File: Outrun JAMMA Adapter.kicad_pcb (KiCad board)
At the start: 2 copper layers, 111 x 77.8 mm, 24 parts, among them U1 LM386, U2 MCP4902, U4 328P

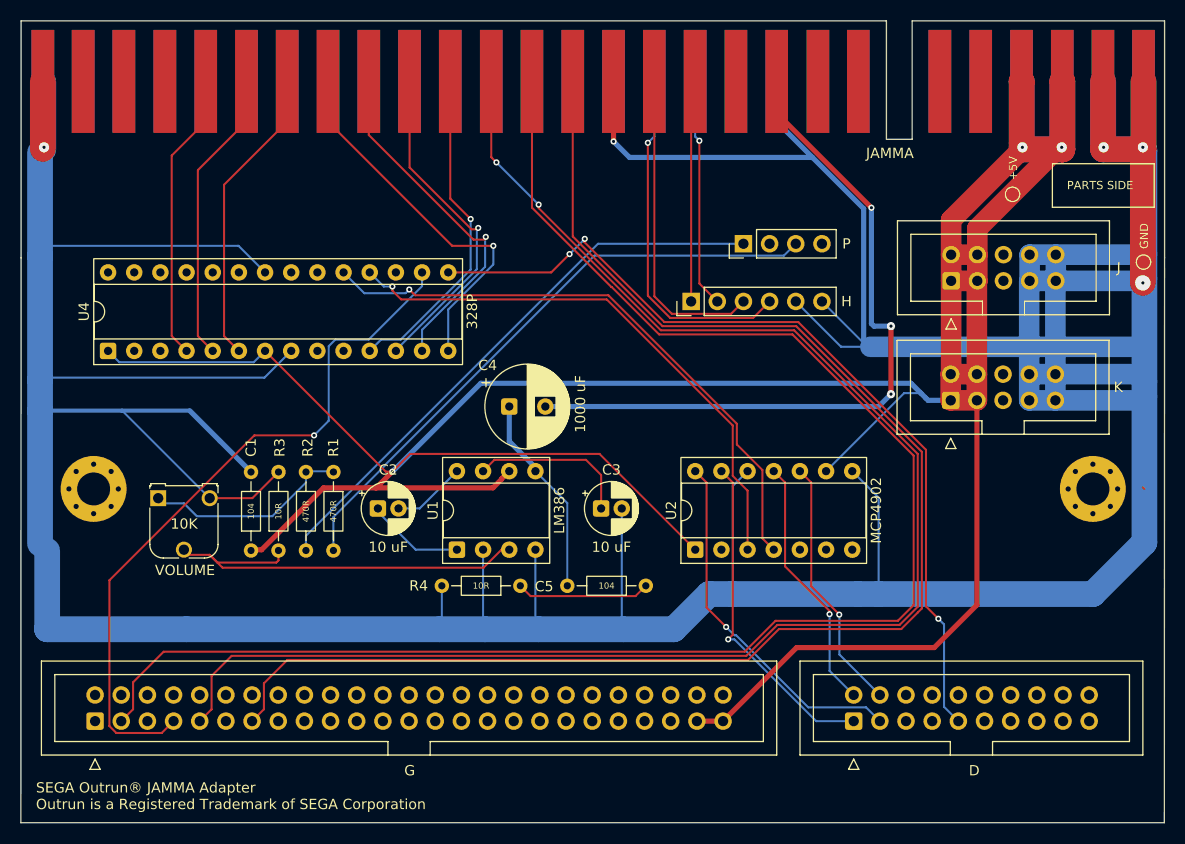
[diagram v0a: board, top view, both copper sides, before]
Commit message: add 100R resistors
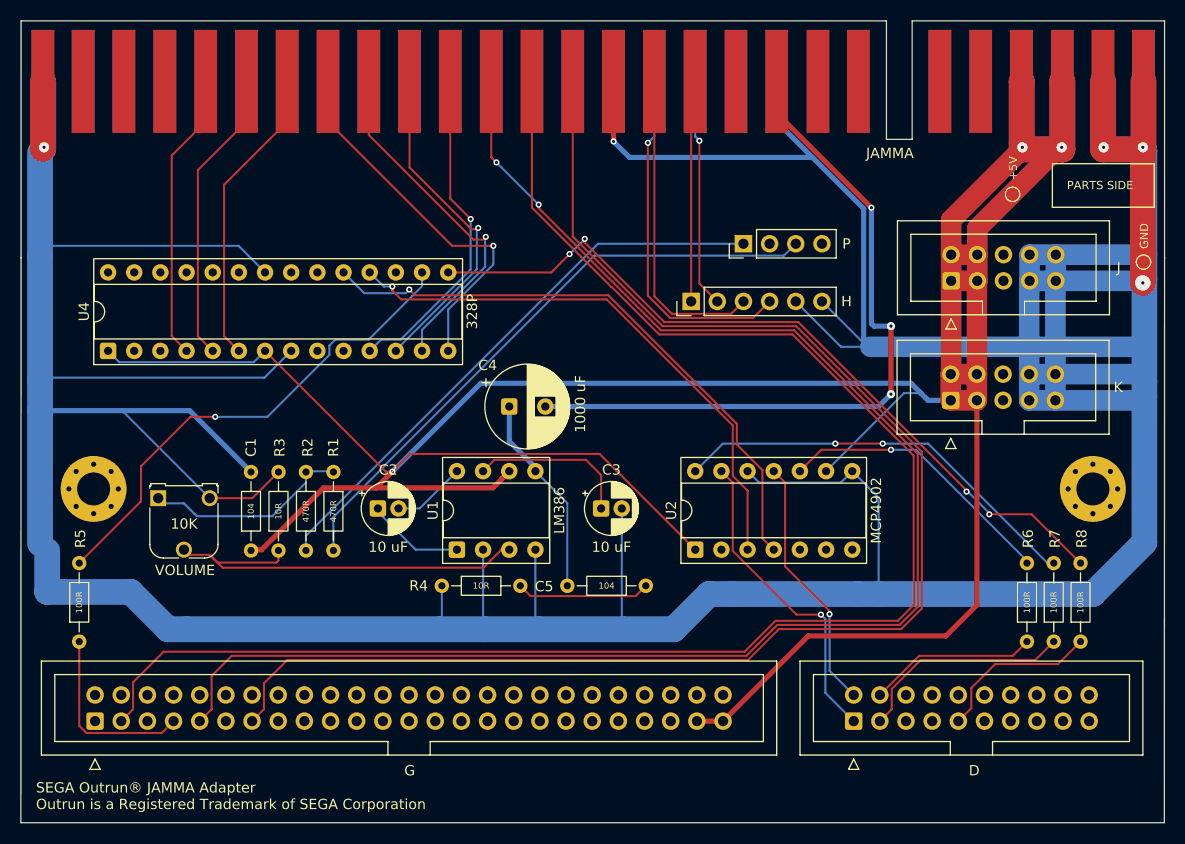
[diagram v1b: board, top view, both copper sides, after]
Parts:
- added R5: 100R, Resistor_THT:R_Axial_DIN0204_L3.6mm_D1.6mm_P7.62mm_Horizontal, F.Cu at (99.6, 123.6)
- added R6: 100R, Resistor_THT:R_Axial_DIN0204_L3.6mm_D1.6mm_P7.62mm_Horizontal, F.Cu at (191.6, 123.6)
- added R7: 100R, Resistor_THT:R_Axial_DIN0204_L3.6mm_D1.6mm_P7.62mm_Horizontal, F.Cu at (194.2, 123.6)
- added R8: 100R, Resistor_THT:R_Axial_DIN0204_L3.6mm_D1.6mm_P7.62mm_Horizontal, F.Cu at (196.8, 123.6)
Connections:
- D pad 3: VOUTA -> ACCEL
- D pad 4: VOUTB -> STEER
- U4 pad 15: BRK -> PB1
- U4 pad 16: SHIFT -> PB2
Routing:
- net PB1: track 0.00 -> 76.2 mm, vias 0 -> 4
- net BRK: track 84.3 -> 16.2 mm, vias 3 -> 0
- net SHIFT: track 68.9 -> 18.3 mm, vias 1 -> 0
- net PB2: track 0.00 -> 48.5 mm, vias 0 -> 1
- net ACCEL: track 0.00 -> 21.2 mm
- net GND: track 593.6 -> 575.9 mm
- net STEER: track 0.00 -> 16.4 mm
- net VOUTA: track 35.1 -> 40.7 mm, vias 1 -> 2
- net VOUTB: track 24.6 -> 27.6 mm
- net REFA: track 32.4 -> 31.0 mm

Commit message: fixes
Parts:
- added C6: 104, Resistor_THT:R_Axial_DIN0204_L3.6mm_D1.6mm_P7.62mm_Horizontal, F.Cu at (98.4, 87.8)
- added C7: 104, Resistor_THT:R_Axial_DIN0204_L3.6mm_D1.6mm_P7.62mm_Horizontal, F.Cu at (179.0, 107.0)
- added R9: 10K, Resistor_THT:R_Axial_DIN0204_L3.6mm_D1.6mm_P7.62mm_Horizontal, F.Cu at (110.0, 98.8)
- renumbered U4 to U3
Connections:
- net SCK renamed U3_SCK_U2_SCK
- net U4_BYPASS renamed U1_BYPASS
- net U4_GAIN_P1 renamed U1_GAIN_P1
- net U4_GAIN_P8 renamed U1_GAIN_P8
- U2 pad 3: MISO-CS -> U3_MOSI_U2_CS
- U2 pad 5: MOSI -> U3_MISO_U2_SDI
- U3 pad 1: +5V -> U3_RSET
- U3 pad 17: (no net) -> U3_MOSI_U2_CS
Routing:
- net U3_MISO_U2_SDI: track 0.00 -> 56.8 mm
- net MISO-CS: track 54.3 -> 0.00 mm, vias 1 -> 0
- net U3_MOSI_U2_CS: track 0.00 -> 52.8 mm, vias 0 -> 1
- net +5V: track 320.3 -> 360.7 mm, vias 3 -> 5
- net GND: track 575.9 -> 593.7 mm
- net U3_RSET: track 0.00 -> 3.91 mm
- net U3_SCK_U2_SCK: track 58.3 -> 58.0 mm, vias 1 -> 0

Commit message: fixes
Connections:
- G pad 11: (no net) -> SERVICE
- JAMMA pad 5: -5V -> (no net)
- JAMMA pad 6: +12V -> (no net)
- JAMMA pad E: -5V -> (no net)
- JAMMA pad F: +12V -> (no net)
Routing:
- net SERVICE: track 0.00 -> 125.9 mm, vias 0 -> 1
- net GND: track 593.7 -> 608.0 mm
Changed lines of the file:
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@@
 			(size 2.2 10)
 			(layers "F.Cu" "F.Mask")
-			(net "-5V")
 		)
 		(pad "6" connect rect
@@
 			(size 2.2 10)
 			(layers "F.Cu" "F.Mask")
-			(net "+12V")
 		)
 		(pad "8" connect rect
@@
 			(size 2.2 10)
 			(layers "B.Cu" "B.Mask")
-			(net "-5V")
 		)
 		(pad "F" connect rect
@@
 			(size 2.2 10)
 			(layers "B.Cu" "B.Mask")
-			(net "+12V")
 		)
 		(pad "J" connect rect
@@
 			(layers "*.Cu" "*.Mask")
 			(remove_unused_layers no)
+			(net "SERVICE")
 		)
 		(pad "12" thru_hole circle
@@
 	)
 	(segment
+		(start 168.02 83.6)
+		(end 175.75 83.6)
+		(width 0.2)
+		(layer "B.Cu")
+		(net "GND")
+	)
+	(segment
 		(start 198.98 75.818851)
 		(end 199.001271 75.840122)
@@
 	)
 	(segment
+		(start 166.62 85)
+		(end 168.02 83.6)
+		(width 0.2)
+		(layer "B.Cu")
+		(net "GND")
+	)
+	(segment
 		(start 194.4 88.6)
 		(end 191.86 88.6)
@@
 	)
 	(segment
-		(start 175.75 81.5925)
+		(start 175.75 83.6)
 		(end 175.75 94.35)
 		(width 0.5)
@@
 	)
 	(segment
+		(start 173.1 83.6)
+		(end 175.75 83.6)
+		(width 0.2)
+		(layer "B.Cu")
+		(net "GND")
+	)
+	(segment
 		(start 115.58 100)
 		(end 95.8 100)
@@
 	)
 	(segment
+		(start 175.75 81.5925)
+		(end 175.75 83.6)
+		(width 0.5)
+		(layer "B.Cu")
+		(net "GND")
+	)
+	(segment
 		(start 144.2 122.421752)
 		(end 152.4 122.421752)
@@
 	)
 	(segment
+		(start 171.7 85)
+		(end 173.1 83.6)
+		(width 0.2)
+		(layer "B.Cu")
+		(net "GND")
+	)
+	(segment
 		(start 191.82 97.66)
 		(end 202.26 97.66)
@@
 	)
 	(segment
-		(start 187.070519 69.281981)
-		(end 187.11 69.2425)
-		(width 0.2)
-		(layer "F.Cu")
-		(net "-5V")
-	)
-	(segment
-		(start 187.070519 69.281981)
-		(end 187.11 69.2425)
-		(width 0.2)
-		(layer "B.Cu")
-		(net "-5V")
-	)
-	(segment
-		(start 183.129592 69.262908)
-		(end 183.15 69.2425)
-		(width 0.2)
-		(layer "B.Cu")
-		(net "+12V")
-	)
-	(segment
 		(start 167.3 69.2425)
 		(end 167.3 72.3)
@@
 	)
 	(segment
+		(start 112.29 132.89)
+		(end 100.29 132.89)
+		(width 0.2)
+		(layer "F.Cu")
+		(net "SERVICE")
+	)
+	(segment
+		(start 97.4 130)
+		(end 97.4 86)
+		(width 0.2)
+		(layer "F.Cu")
+		(net "SERVICE")
+	)
+	(segment
+		(start 97.4 86)
+		(end 102.6 80.8)
+		(width 0.2)
+		(layer "F.Cu")
+		(net "SERVICE")
+	)
+	(segment
+		(start 100.29 132.89)
+		(end 97.4 130)
+		(width 0.2)
+		(layer "F.Cu")
+		(net "SERVICE")
+	)
+	(segment
+		(start 113.84 131.34)
+		(end 112.29 132.89)
+		(width 0.2)
+		(layer "F.Cu")
+		(net "SERVICE")
+	)
+	(via
+		(at 102.6 80.8)
+		(size 0.6)
+		(drill 0.3)
+		(layers "F.Cu" "B.Cu")
+		(net "SERVICE")
+	)
+	(segment
+		(start 151.47 73.73)
+		(end 151.47 69.2425)
+		(width 0.2)
+		(layer "B.Cu")
+		(net "SERVICE")
+	)
+	(segment
+		(start 107 76.4)
+		(end 148.8 76.4)
+		(width 0.2)
+		(layer "B.Cu")
+		(net "SERVICE")
+	)
+	(segment
+		(start 102.6 80.8)
+		(end 107 76.4)
+		(width 0.2)
+		(layer "B.Cu")
+		(net "SERVICE")
+	)
+	(segment
+		(start 148.8 76.4)
+		(end 151.47 73.73)
+		(width 0.2)
+		(layer "B.Cu")
+		(net "SERVICE")
+	)
+	(segment
 		(start 186.2 128.115525)
 		(end 186.2 130.08)
@@
 	)
 	(segment
-		(start 100.305256 132.49)
-		(end 107.61 132.49)
+		(start 102.29 132.174744)
+		(end 102.605256 132.49)
+		(width 0.2)
+		(layer "F.Cu")
+		(net "SHIFT")
+	)
+	(segment
+		(start 102.29 130.505256)
+		(end 102.29 132.174744)
+		(width 0.2)
+		(layer "F.Cu")
+		(net "SHIFT")
+	)
+	(segment
+		(start 99.6 129.484744)
+		(end 100.305256 130.19)
 		(width 0.2)
 		(layer "F.Cu")
@@
 	)
 	(segment
+		(start 102.605256 132.49)
+		(end 107.61 132.49)
+		(width 0.2)
+		(layer "F.Cu")
+		(net "SHIFT")
+	)
+	(segment
 		(start 99.6 123.4)
-		(end 99.6 131.784744)
+		(end 99.6 129.484744)
+		(width 0.2)
+		(layer "F.Cu")
+		(net "SHIFT")
+	)
+	(segment
+		(start 100.305256 130.19)
+		(end 101.974744 130.19)
 		(width 0.2)
 		(layer "F.Cu")
@@
 	)
 	(segment
-		(start 99.6 131.784744)
-		(end 100.305256 132.49)
+		(start 101.974744 130.19)
+		(end 102.29 130.505256)
 		(width 0.2)
 		(layer "F.Cu")

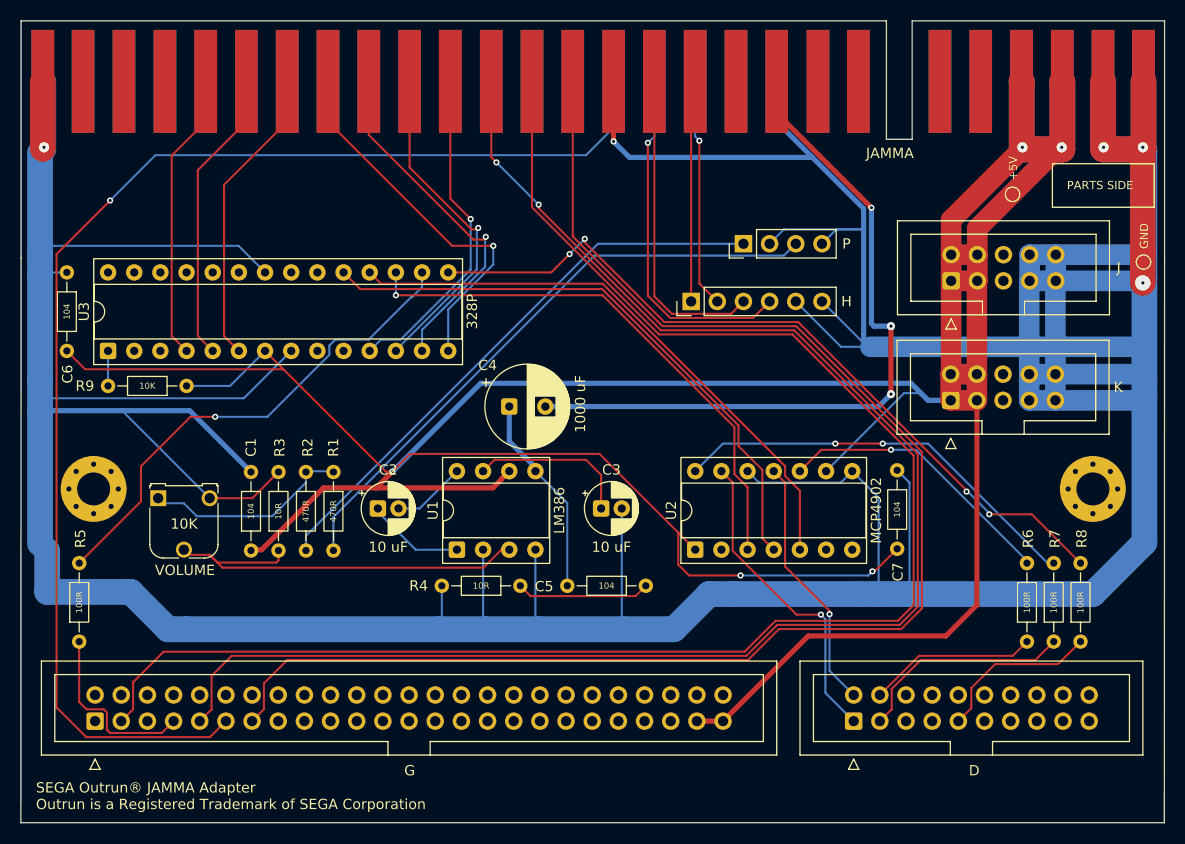
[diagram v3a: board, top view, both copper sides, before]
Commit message: reverse A/B on AMP50 and AMP20
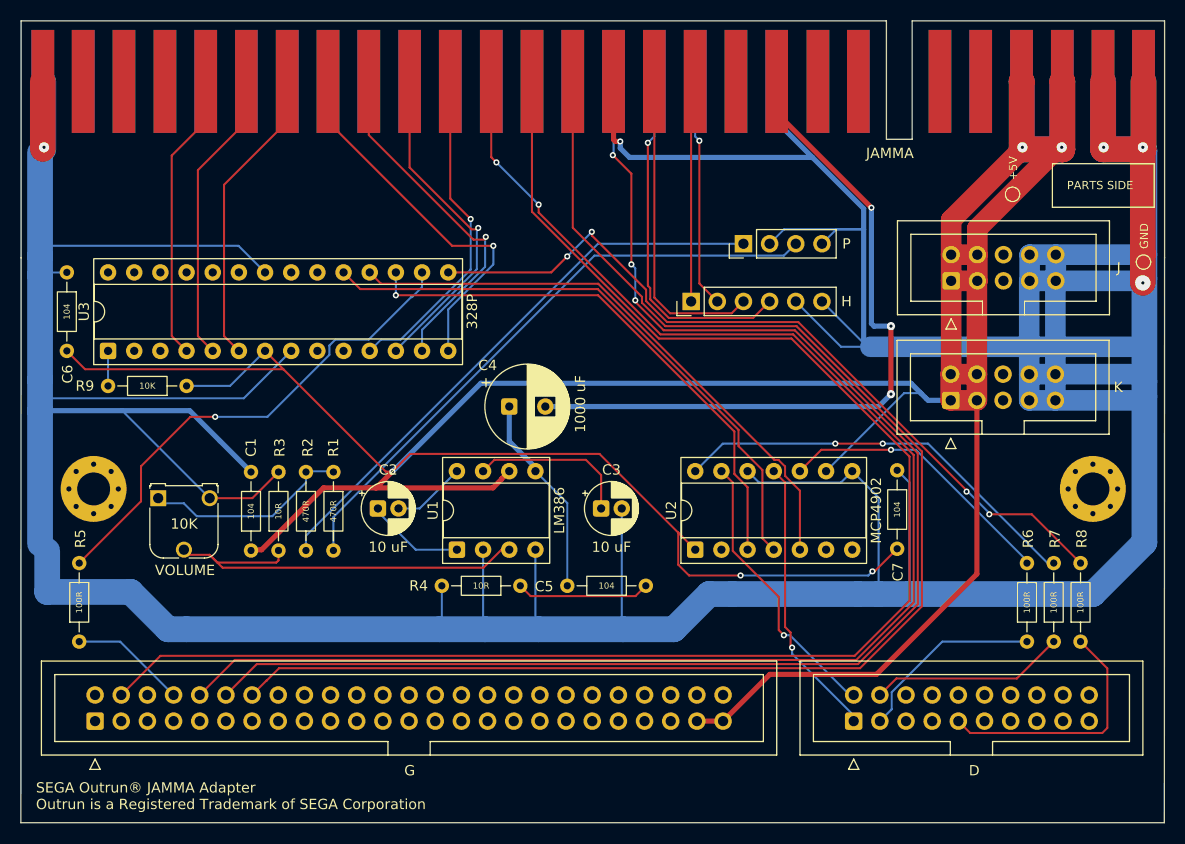
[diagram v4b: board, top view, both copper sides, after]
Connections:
- D pad 1: REFA -> REFB
- D pad 2: REFB -> REFA
- D pad 3: ACCEL -> STEER
- D pad 4: STEER -> ACCEL
- G pad 10: (no net) -> 1P_START
- G pad 11: SERVICE -> (no net)
- G pad 12: (no net) -> SERVICE
- G pad 13: TEST -> (no net)
- G pad 14: (no net) -> TEST
- G pad 3: COIN_1 -> (no net)
- G pad 4: (no net) -> COIN_1
- G pad 7: SHIFT -> (no net)
- G pad 8: (no net) -> SHIFT
- G pad 9: 1P_START -> (no net)
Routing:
- net SERVICE: track 125.9 -> 141.3 mm, vias 1 -> 3
- net BRK: track 16.2 -> 24.6 mm
- net SHIFT: track 17.9 -> 11.3 mm
- net 1P_START: track 151.9 -> 148.1 mm
- net COIN_1: track 156.9 -> 153.4 mm
- net REFA: track 31.0 -> 27.6 mm
- net TEST: track 143.8 -> 141.0 mm
- net REFB: track 24.9 -> 27.5 mm
- net ACCEL: track 21.2 -> 19.0 mm
- net STEER: track 16.4 -> 18.5 mm
- net +5V: track 360.7 -> 359.0 mm
- net PB1: track 76.2 -> 77.3 mm
